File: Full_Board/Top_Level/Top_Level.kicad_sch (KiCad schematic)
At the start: 7 parts, among them J1 OQ0212500000G, J2 OQ0212500000G, J3 OQ0432500000G, J4 OQ0432500000G, J5 OQ0432500000G

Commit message: Working on power supply
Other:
- added sheet Signal Light (Status_Light_Subsystem/signal_light.kicad_sch)
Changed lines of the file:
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@@
+    )
+  )
+  (sheet (at 114.3 176.53) (size 17.78 15.24) (fields_autoplaced)
+    (stroke (width 0.1524) (type solid) (color 0 0 0 0))
+    (fill (color 0 0 0 0.0000))
+    (property "Sheet name" "Signal Light" (id 0) (at 114.3 175.8184 0)
+      (effects (font (size 1.27 1.27)) (justify left bottom))
+    )
+    (property "Sheet file" "Status_Light_Subsystem/signal_light.kicad_sch" (id 1) (at 114.3 192.3546 0)
+      (effects (font (size 1.27 1.27)) (justify left top) hide)
     )
   )
@@
     (path "/07cad15c-7a8f-4f19-b010-f610659ec73e" (page "18"))
     (path "/052c1802-f400-4007-8083-56d46632424e" (page "19"))
+    (path "/ff9e0524-8334-47df-91dd-f4ed6e05afe2" (page "23"))
   )
   (symbol_instances

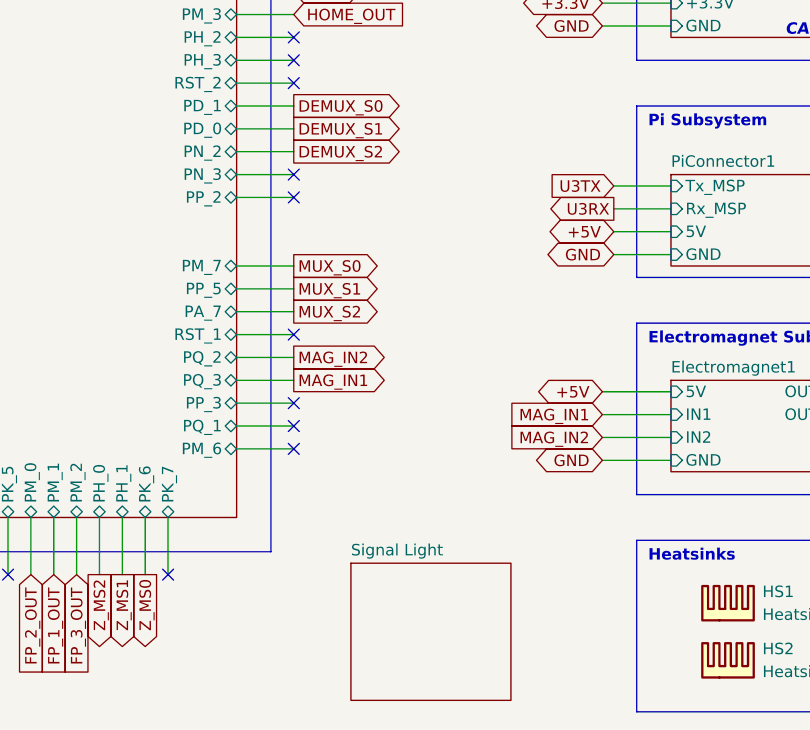
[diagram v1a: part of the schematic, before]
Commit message: Added signal light MOSFET
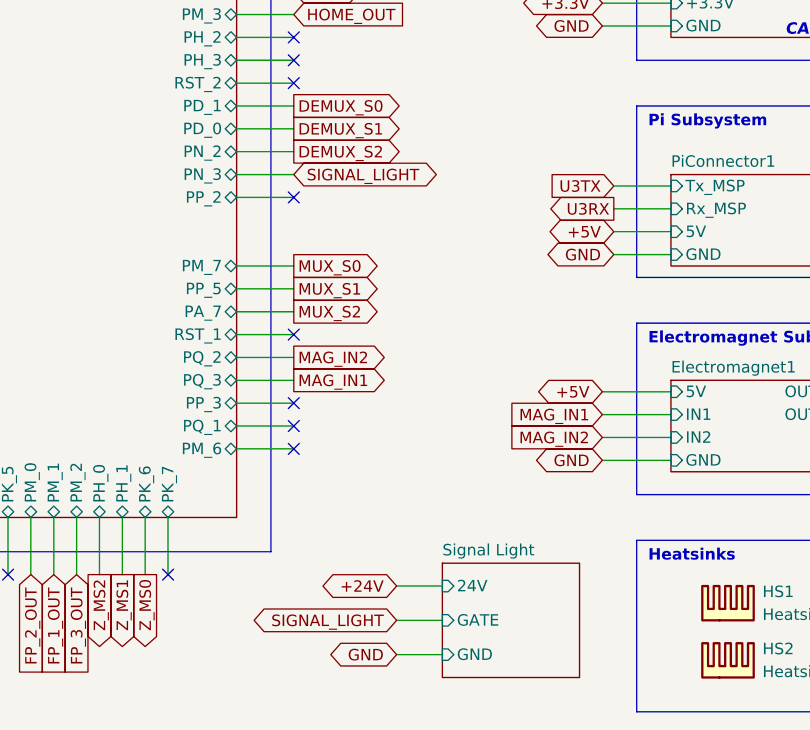
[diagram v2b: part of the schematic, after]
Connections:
- no-connect marks 25 -> 24
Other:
- sheet Signal Light: file Status_Light_Subsystem/signal_light.kicad_sch -> ../Signal_Light_Subsystem/Signal_Light.kicad_sch
- sheet Signal Light ports: added 24V, GATE, GND; removed none

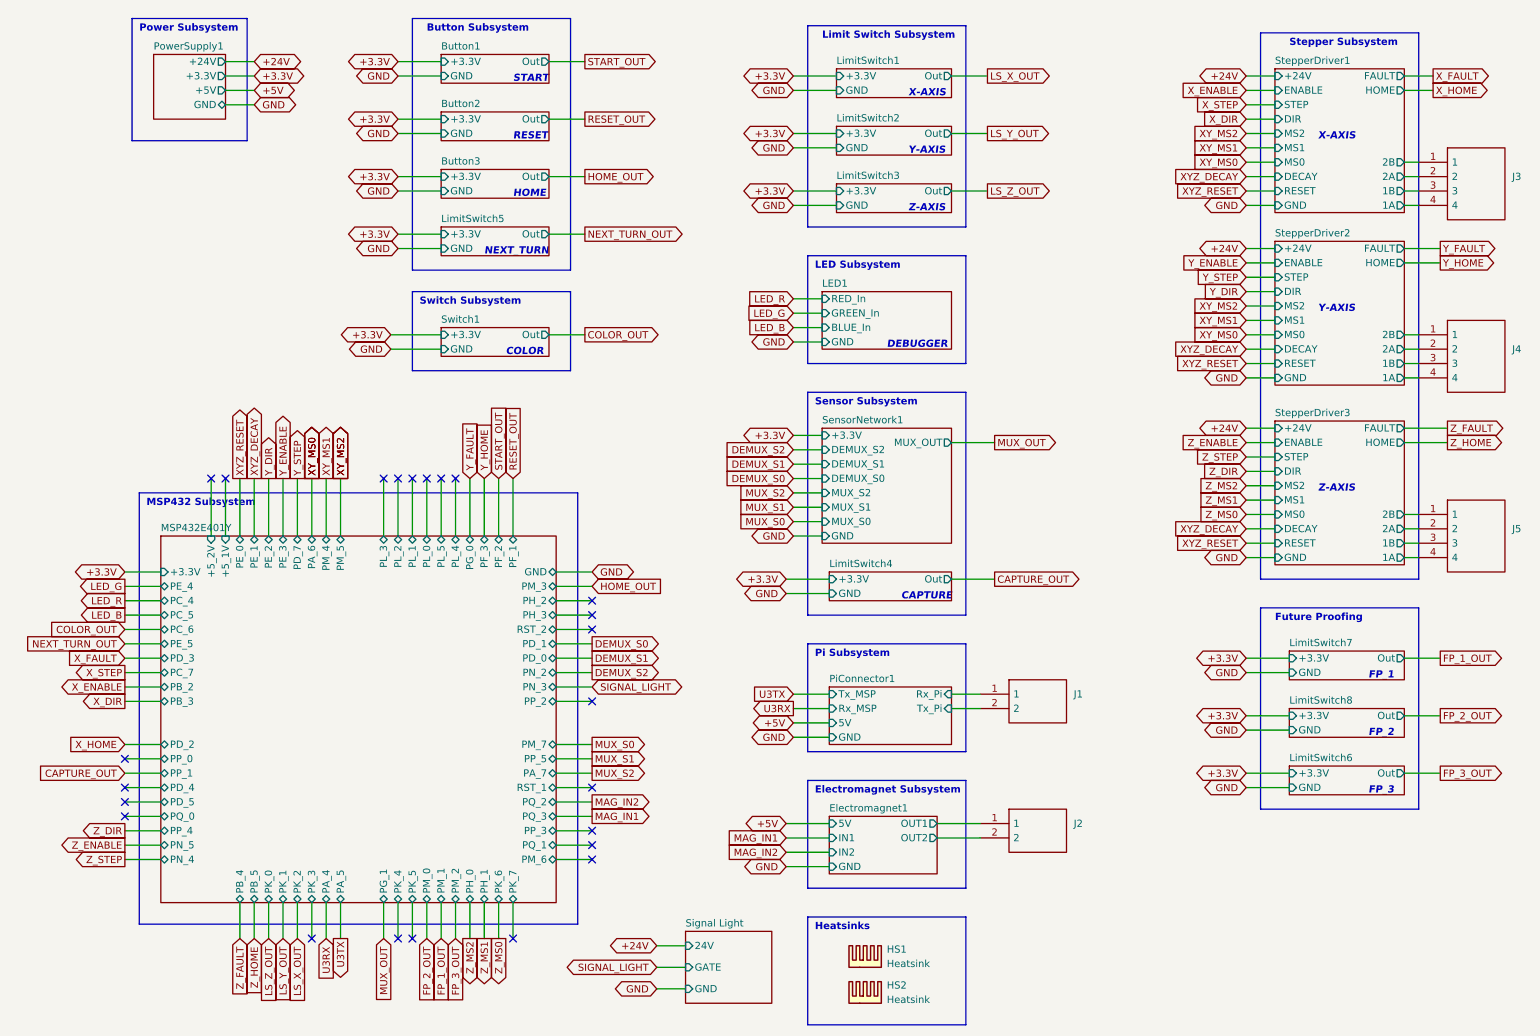
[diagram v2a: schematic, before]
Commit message: Replace small resistors/capacitors with through-hole; fix DRC aside from electromagnet and MUXes
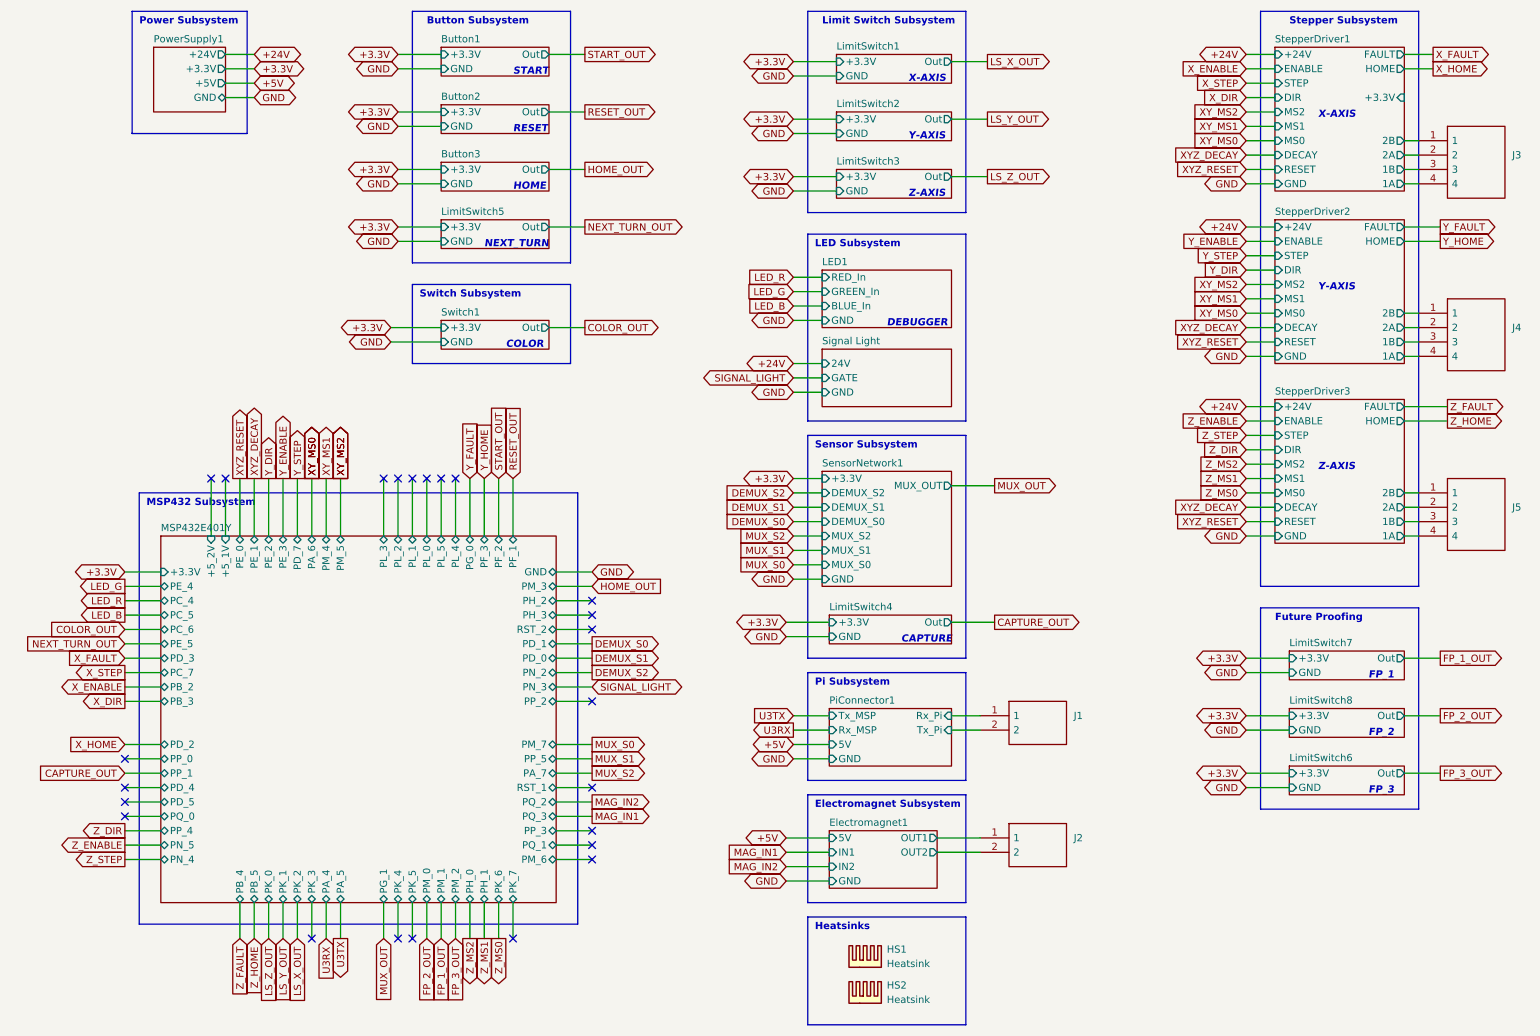
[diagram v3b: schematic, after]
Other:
- sheet StepperDriver1 ports: added +3.3V; removed none
- moved on the sheet: J1, J2, J3, J4, J5

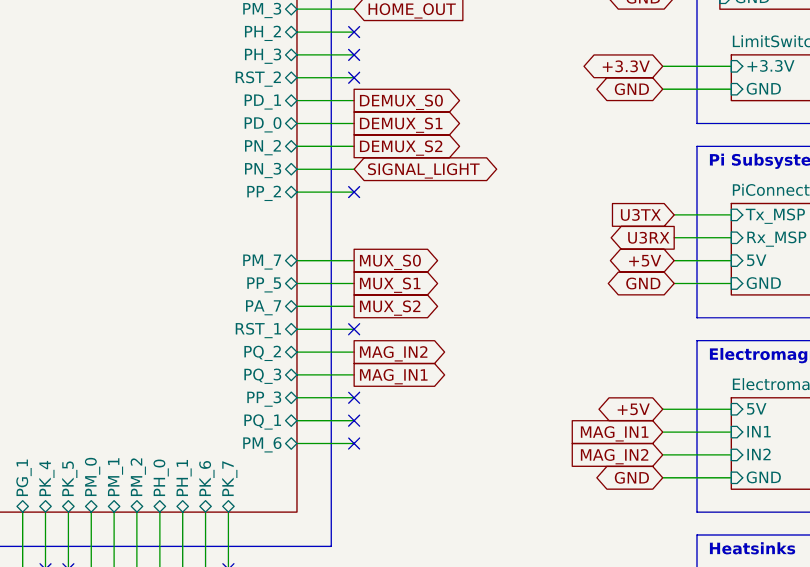
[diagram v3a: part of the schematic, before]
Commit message: Replace MUX/DEMUX; DRC passes aside from electromagnet
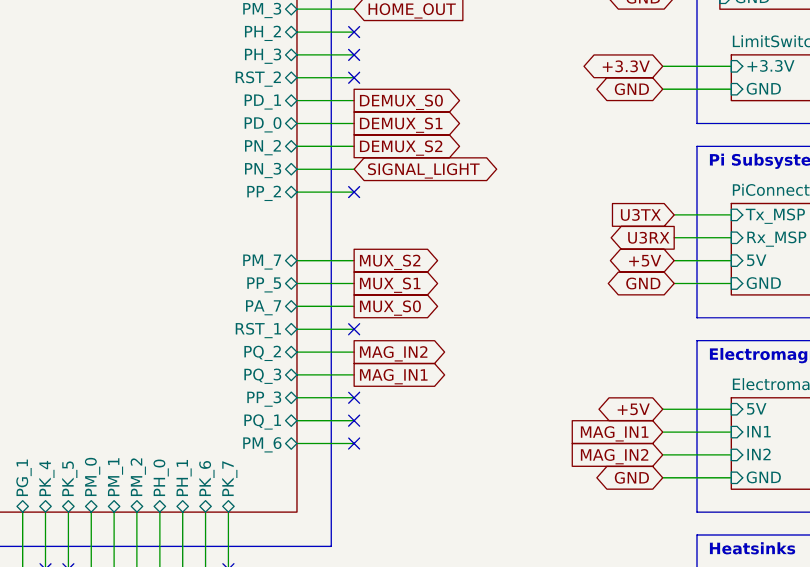
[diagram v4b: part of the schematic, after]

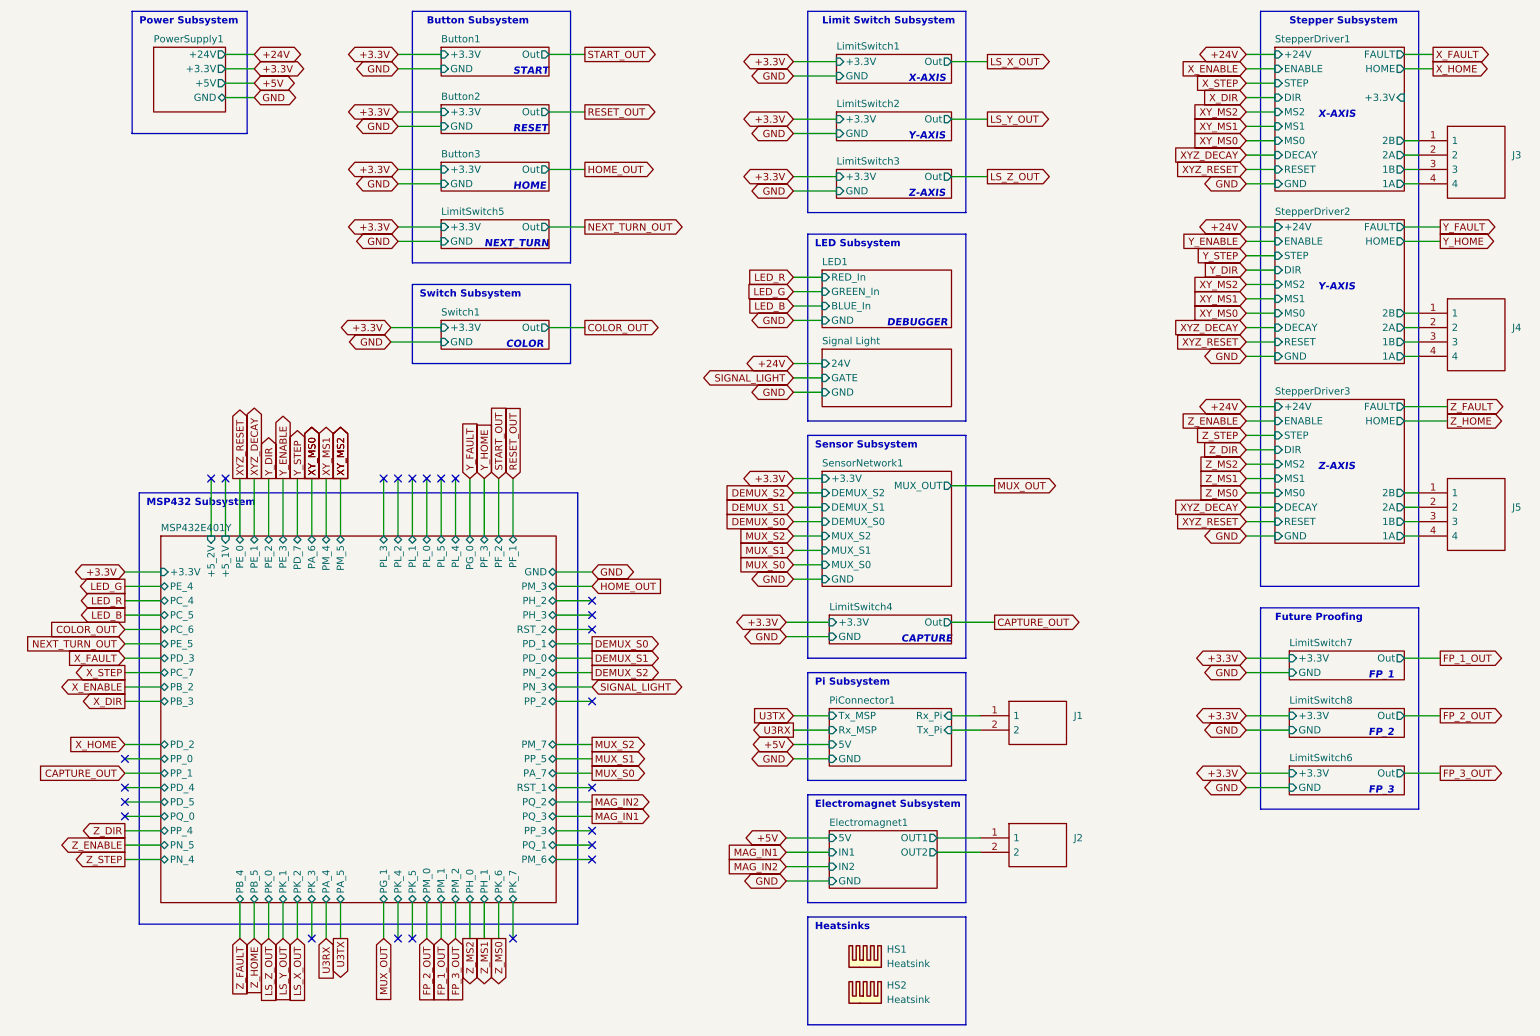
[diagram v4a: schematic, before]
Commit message: Replaced electromagnet IC and fixed ERC errors with stepper driver
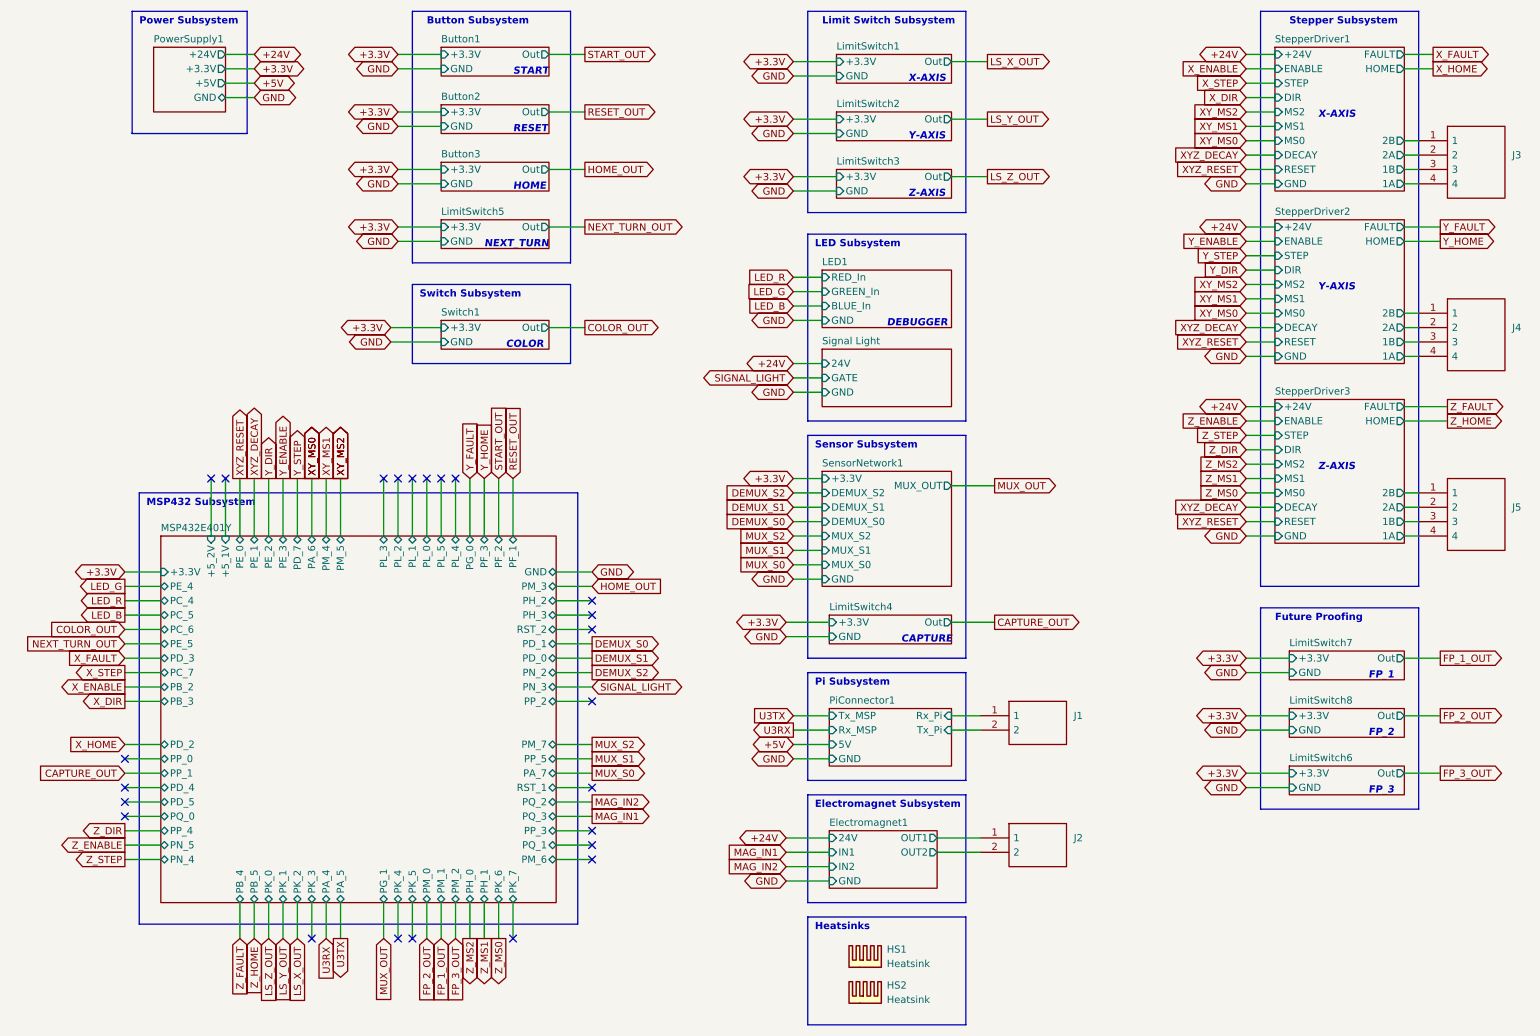
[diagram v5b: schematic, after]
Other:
- sheet Electromagnet1 ports: added 24V; removed 5V
- sheet StepperDriver1 ports: added none; removed +3.3V
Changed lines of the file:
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@@
+    )
+  )
+  (global_label "+24V" (shape bidirectional) (at 142.24 160.02 180) (fields_autoplaced)
+    (effects (font (size 1.27 1.27)) (justify right))
+    (property "Intersheet References" "${INTERSHEET_REFS}" (id 0) (at 134.7469 160.0994 0)
+      (effects (font (size 1.27 1.27)) (justify right) hide)
     )
   )
@@
     (effects (font (size 1.27 1.27)) (justify right))
     (property "Intersheet References" "${INTERSHEET_REFS}" (id 0) (at 217.2364 130.8894 0)
-      (effects (font (size 1.27 1.27)) (justify right) hide)
-    )
-  )
-  (global_label "+5V" (shape bidirectional) (at 142.24 160.02 180) (fields_autoplaced)
-    (effects (font (size 1.27 1.27)) (justify right))
-    (property "Intersheet References" "${INTERSHEET_REFS}" (id 0) (at 135.9564 160.0994 0)
       (effects (font (size 1.27 1.27)) (justify right) hide)
     )
@@
       (effects (font (size 1.27 1.27)) (justify left))
     )
-    (pin "+3.3V" input (at 251.46 29.21 0)
-      (effects (font (size 1.27 1.27)) (justify right))
-    )
   )
   (sheet (at 149.86 120.65) (size 21.59 5.08) (fields_autoplaced)
@@
       (effects (font (size 1.27 1.27)) (justify left top) hide)
     )
-    (pin "5V" input (at 149.86 160.02 180)
-      (effects (font (size 1.27 1.27)) (justify left))
-    )
     (pin "OUT2" output (at 168.91 162.56 0)
       (effects (font (size 1.27 1.27)) (justify right))
@@
     )
     (pin "IN1" input (at 149.86 162.56 180)
+      (effects (font (size 1.27 1.27)) (justify left))
+    )
+    (pin "24V" input (at 149.86 160.02 180)
       (effects (font (size 1.27 1.27)) (justify left))
     )
@@
       (reference "#FLG06") (unit 1) (value "PWR_FLAG") (footprint "")
     )
+    (path "/b2aa64e3-6d16-4ba0-adea-08cdcba55275/2cdca297-89d2-4945-b79e-3756b5d25bbb"
+      (reference "#FLG0101") (unit 1) (value "PWR_FLAG") (footprint "")
+    )
+    (path "/b2aa64e3-6d16-4ba0-adea-08cdcba55275/a39d3bb3-367b-459b-90b7-753632cfa817"
+      (reference "#FLG0102") (unit 1) (value "PWR_FLAG") (footprint "")
+    )
     (path "/a91d8bd8-894f-452b-99c8-57023ebaf362/8c133614-4038-4102-86b6-14eb1a71595f"
       (reference "C1") (unit 1) (value "100 uF") (footprint "Capacitor_THT:C_Radial_D6.3mm_H5.0mm_P2.50mm")
@@
       (reference "IC4") (unit 1) (value "LM2576HVS-5.0_NOPB") (footprint "LM2576HVS50NOPB")
     )
-    (path "/f059198e-ec55-48b1-bb71-d05bde55edab/d3b563d6-69a8-4f35-9b31-a733b771995f"
-      (reference "IC5") (unit 1) (value "DRV8210DRLR") (footprint "SOTFL50P160X60-6N")
+    (path "/f059198e-ec55-48b1-bb71-d05bde55edab/c9b392ca-4c7a-4289-94e7-3f89c24e8fe4"
+      (reference "IC5") (unit 1) (value "BD62130AEFJ-E2") (footprint "SOIC127P600X100-9N")
     )
     (path "/c49c40d9-3b05-4cae-a1f5-15f0abbbf620"
